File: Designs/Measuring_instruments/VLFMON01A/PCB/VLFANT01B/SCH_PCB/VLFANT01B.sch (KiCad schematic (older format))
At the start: 15 parts, among them J1 RJ45_RJHSE-5384, J2 RJ45_RJHSE-5384, J3 RJ45_RJHSE-5384, J7 SMA, J9 JUMP_3X2, M1 HOLE, M10 HOLE, M2 HOLE, M3 HOLE, M4 HOLE, M5 HOLE, M6 HOLE, M7 HOLE, M8 HOLE, M9 HOLE

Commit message: zmena
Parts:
- removed M10, M5, M6, M7, M8, M9: HOLE, Mlab_Mechanical:MountingHole_3mm, symbol HOLE
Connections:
- net OUT1: now also J3.4; no longer J3.1
- net OUT2: now also J3.5; no longer J3.2
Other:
- moved on the sheet: M1, M2, M3, M4

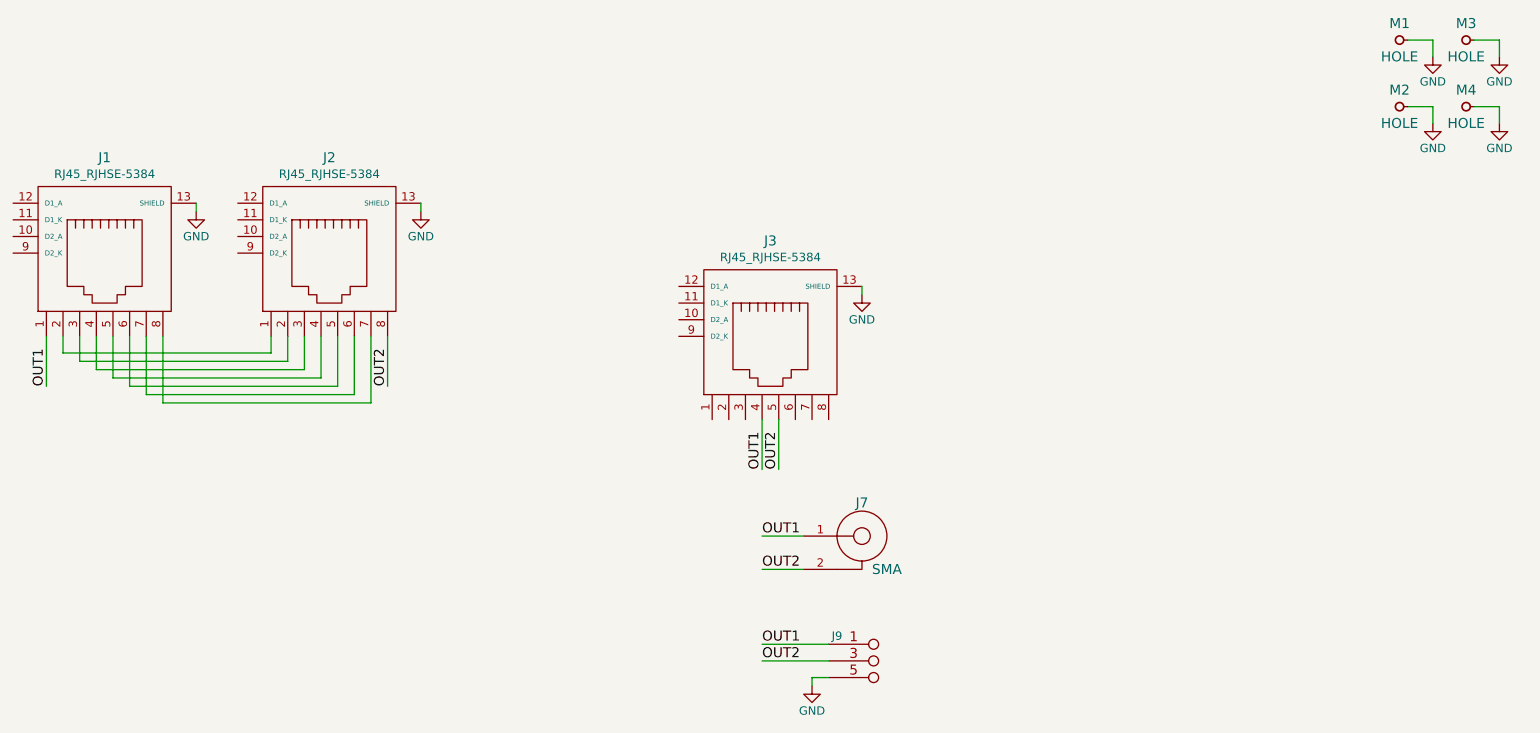
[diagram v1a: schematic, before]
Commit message: 
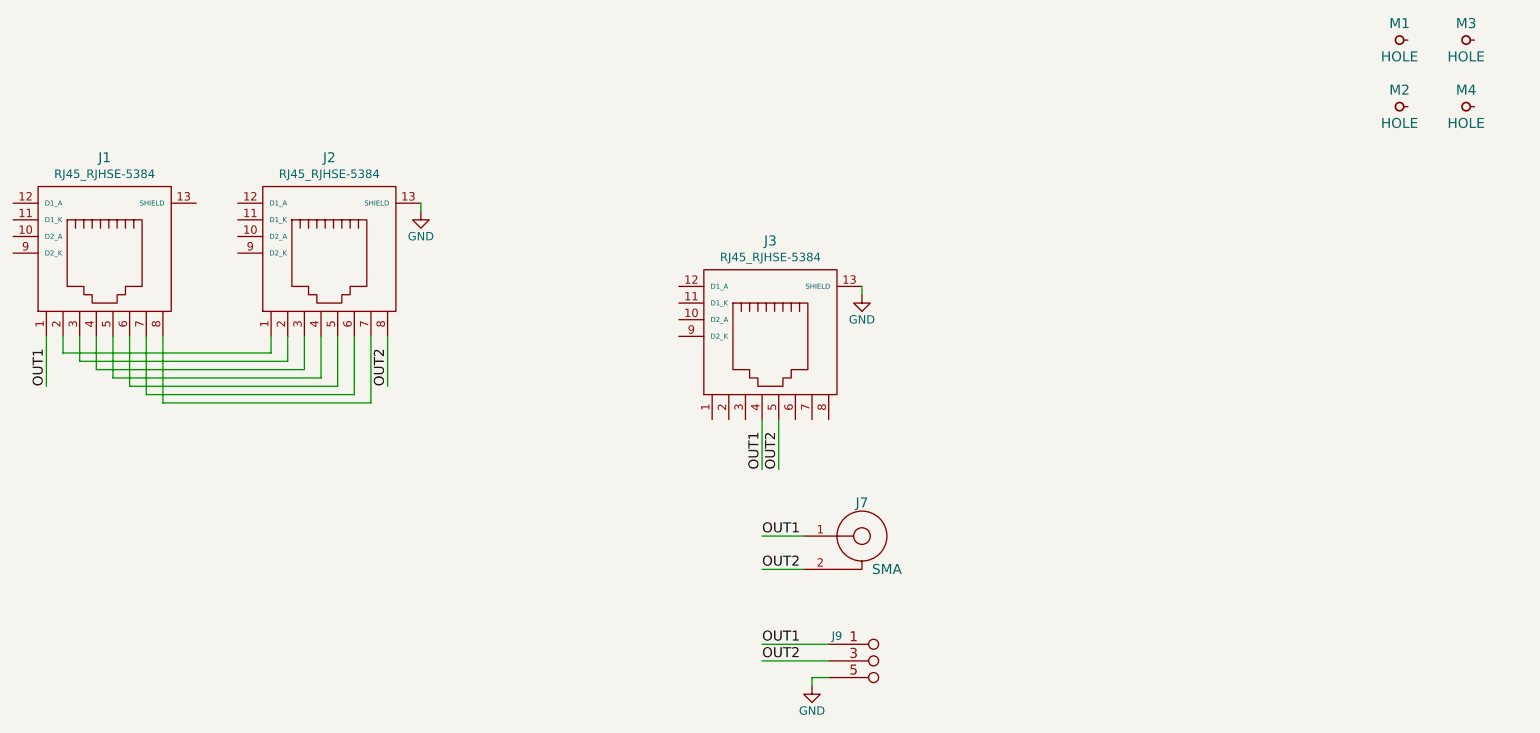
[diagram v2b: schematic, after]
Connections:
- net GND: no longer J1.13 (SHIELD), M1.1, M2.1, M3.1, M4.1
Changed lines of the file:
@@
 EESchema Schematic File Version 2
+LIBS:MLAB_BATERY
+LIBS:MLAB_CONNECTORS
+LIBS:MLAB_D
+LIBS:MLAB_DISPLAY
+LIBS:MLAB_IO
+LIBS:MLAB_Jumpers
+LIBS:MLAB_SW
+LIBS:MLAB_T
+LIBS:MLAB_U
 LIBS:74xgxx
 LIBS:74xx
-LIBS:ac-dc
 LIBS:actel
 LIBS:adc-dac
@@
 LIBS:brooktre
 LIBS:cmos4000
-LIBS:cmos_ieee
 LIBS:conn
 LIBS:contrib
@@
 LIBS:display
 LIBS:dsp
-LIBS:elec-unifil
 LIBS:ESD_Protection
 LIBS:ftdi
 LIBS:gennum
-LIBS:graphic
 LIBS:hc11
 LIBS:intel
@@
 LIBS:microchip_pic32mcu
 LIBS:microcontrollers
+LIBS:mlab_header
+LIBS:mlab_mechanical
 LIBS:motor_drivers
 LIBS:motorola
@@
 LIBS:transf
 LIBS:transistors
-LIBS:ttl_ieee
 LIBS:valves
 LIBS:video
 LIBS:Xicor
-LIBS:xilinx
 LIBS:Zilog
 LIBS:VLFANT01B-cache
@@
 $EndComp
 $Comp
-L GND #PWR01
-U 1 1 57D29BFA
-P 10480 820
-F 0 "#PWR01" H 10480 570 50  0001 C CNN
-F 1 "GND" H 10480 670 50  0000 C CNN
-F 2 "" H 10480 820 50  0000 C CNN
-F 3 "" H 10480 820 50  0000 C CNN
-	1    10480 820
-	1    0    0    -1
-$EndComp
-$Comp
 L HOLE M3
 U 1 1 57D2A075
@@
 $EndComp
 $Comp
-L GND #PWR02
-U 1 1 57D2A07B
-P 10880 820
-F 0 "#PWR02" H 10880 570 50  0001 C CNN
-F 1 "GND" H 10880 670 50  0000 C CNN
-F 2 "" H 10880 820 50  0000 C CNN
-F 3 "" H 10880 820 50  0000 C CNN
-	1    10880 820
-	1    0    0    -1
-$EndComp
-$Comp
 L HOLE M2
 U 1 1 57D2A387
@@
 $EndComp
 $Comp
-L GND #PWR03
-U 1 1 57D2A38D
-P 10480 1220
-F 0 "#PWR03" H 10480 970 50  0001 C CNN
-F 1 "GND" H 10480 1070 50  0000 C CNN
-F 2 "" H 10480 1220 50  0000 C CNN
-F 3 "" H 10480 1220 50  0000 C CNN
-	1    10480 1220
-	1    0    0    -1
-$EndComp
-$Comp
 L HOLE M4
 U 1 1 57D2A395
@@
 $EndComp
 $Comp
-L GND #PWR04
-U 1 1 57D2A39B
-P 10880 1220
-F 0 "#PWR04" H 10880 970 50  0001 C CNN
-F 1 "GND" H 10880 1070 50  0000 C CNN
-F 2 "" H 10880 1220 50  0000 C CNN
-F 3 "" H 10880 1220 50  0000 C CNN
-	1    10880 1220
-	1    0    0    -1
-$EndComp
-Wire Wire Line
-	10330 720  10480 720
-Wire Wire Line
-	10480 720  10480 820
-Wire Wire Line
-	10730 720  10880 720
-Wire Wire Line
-	10880 720  10880 820
-Wire Wire Line
-	10330 1120 10480 1120
-Wire Wire Line
-	10480 1120 10480 1220
-Wire Wire Line
-	10730 1120 10880 1120
-Wire Wire Line
-	10880 1120 10880 1220
-$Comp
 L SMA J7
 U 1 1 57D68C46
@@
 	6750 4550 6850 4550
 $Comp
+L RJ45_RJHSE-5384 J2
+U 1 1 58171334
+P 3850 2050
+F 0 "J2" H 3850 2674 60  0000 C CNN
+F 1 "RJ45_RJHSE-5384" H 3850 2575 51  0000 C CNN
+F 2 "Mlab_CON:RJHSE-5384(RJ45)" H 3850 2050 60  0001 C CNN
+F 3 "" H 3850 2050 60  0000 C CNN
+	1    3850 2050
+	1    0    0    -1
+$EndComp
+$Comp
+L RJ45_RJHSE-5384 J3
+U 1 1 58171450
+P 6500 2550
+F 0 "J3" H 6500 3174 60  0000 C CNN
+F 1 "RJ45_RJHSE-5384" H 6500 3075 51  0000 C CNN
+F 2 "Mlab_CON:RJHSE-5384(RJ45)" H 6500 2550 60  0001 C CNN
+F 3 "" H 6500 2550 60  0000 C CNN
+	1    6500 2550
+	1    0    0    -1
+$EndComp
+Text Label 2150 2800 1    60   ~ 0
+OUT1
+Wire Wire Line
+	2150 2500 2150 2800
+Wire Wire Line
+	3500 2500 3500 2600
+Wire Wire Line
+	3500 2600 2250 2600
+Wire Wire Line
+	2250 2600 2250 2500
+Wire Wire Line
+	3600 2500 3600 2650
+Wire Wire Line
+	3600 2650 2350 2650
+Wire Wire Line
+	2350 2650 2350 2500
+Wire Wire Line
+	3700 2500 3700 2700
+Wire Wire Line
+	3700 2700 2450 2700
+Wire Wire Line
+	2450 2700 2450 2500
+Wire Wire Line
+	3800 2500 3800 2750
+Wire Wire Line
+	3800 2750 2550 2750
+Wire Wire Line
+	2550 2750 2550 2500
+Wire Wire Line
+	3900 2500 3900 2800
+Wire Wire Line
+	3900 2800 2650 2800
+Wire Wire Line
+	2650 2800 2650 2500
+Wire Wire Line
+	4000 2500 4000 2850
+Wire Wire Line
+	4000 2850 2750 2850
+Wire Wire Line
+	2750 2850 2750 2500
+Wire Wire Line
+	4100 2500 4100 2900
+Wire Wire Line
+	4100 2900 2850 2900
+Wire Wire Line
+	2850 2900 2850 2500
+Text Label 4200 2800 1    60   ~ 0
+OUT2
+Wire Wire Line
+	4200 2500 4200 2800
+$Comp
+L GND #PWR013
+U 1 1 581734D2
+P 4400 1750
+F 0 "#PWR013" H 4400 1500 50  0001 C CNN
+F 1 "GND" H 4400 1600 50  0000 C CNN
+F 2 "" H 4400 1750 50  0000 C CNN
+F 3 "" H 4400 1750 50  0000 C CNN
+	1    4400 1750
+	1    0    0    -1
+$EndComp
+Wire Wire Line
+	4400 1750 4400 1700
+Text Label 6450 3300 1    60   ~ 0
+OUT1
+Text Label 6550 3300 1    60   ~ 0
+OUT2
+Wire Wire Line
+	6450 3300 6450 3000
+Wire Wire Line
+	6550 3300 6550 3000
+$Comp
+L GND #PWR014
+U 1 1 581755DF
+P 7050 2250
+F 0 "#PWR014" H 7050 2000 50  0001 C CNN
+F 1 "GND" H 7050 2100 50  0000 C CNN
+F 2 "" H 7050 2250 50  0000 C CNN
+F 3 "" H 7050 2250 50  0000 C CNN
+	1    7050 2250
+	1    0    0    -1
+$EndComp
+Wire Wire Line
+	7050 2250 7050 2200
+$Comp
 L RJ45_RJHSE-5384 J1
 U 1 1 58170EC6
@@
 	1    0    0    -1
 $EndComp
-$Comp
-L RJ45_RJHSE-5384 J2
-U 1 1 58171334
-P 3850 2050
-F 0 "J2" H 3850 2674 60  0000 C CNN
-F 1 "RJ45_RJHSE-5384" H 3850 2575 51  0000 C CNN
-F 2 "Mlab_CON:RJHSE-5384(RJ45)" H 3850 2050 60  0001 C CNN
-F 3 "" H 3850 2050 60  0000 C CNN
-	1    3850 2050
-	1    0    0    -1
-$EndComp
-$Comp
-L RJ45_RJHSE-5384 J3
-U 1 1 58171450
-P 6500 2550
-F 0 "J3" H 6500 3174 60  0000 C CNN
-F 1 "RJ45_RJHSE-5384" H 6500 3075 51  0000 C CNN
-F 2 "Mlab_CON:RJHSE-5384(RJ45)" H 6500 2550 60  0001 C CNN
-F 3 "" H 6500 2550 60  0000 C CNN
-	1    6500 2550
-	1    0    0    -1
-$EndComp
-Text Label 2150 2800 1    60   ~ 0
-OUT1
-Wire Wire Line
-	2150 2500 2150 2800
-Wire Wire Line
-	3500 2500 3500 2600
-Wire Wire Line
-	3500 2600 2250 2600
-Wire Wire Line
-	2250 2600 2250 2500
-Wire Wire Line
-	3600 2500 3600 2650
-Wire Wire Line
-	3600 2650 2350 2650
-Wire Wire Line
-	2350 2650 2350 2500
-Wire Wire Line
-	3700 2500 3700 2700
-Wire Wire Line
-	3700 2700 2450 2700
-Wire Wire Line
-	2450 2700 2450 2500
-Wire Wire Line
-	3800 2500 3800 2750
-Wire Wire Line
-	3800 2750 2550 2750
-Wire Wire Line
-	2550 2750 2550 2500
-Wire Wire Line
-	3900 2500 3900 2800
-Wire Wire Line
-	3900 2800 2650 2800
-Wire Wire Line
-	2650 2800 2650 2500
-Wire Wire Line
-	4000 2500 4000 2850
-Wire Wire Line
-	4000 2850 2750 2850
-Wire Wire Line
-	2750 2850 2750 2500
-Wire Wire Line
-	4100 2500 4100 2900
-Wire Wire Line
-	4100 2900 2850 2900
-Wire Wire Line
-	2850 2900 2850 2500
-Text Label 4200 2800 1    60   ~ 0
-OUT2
-Wire Wire Line
-	4200 2500 4200 2800
-$Comp
-L GND #PWR012
-U 1 1 58173397
-P 3050 1750
-F 0 "#PWR012" H 3050 1500 50  0001 C CNN
-F 1 "GND" H 3050 1600 50  0000 C CNN
-F 2 "" H 3050 1750 50  0000 C CNN
-F 3 "" H 3050 1750 50  0000 C CNN
-	1    3050 1750
-	1    0    0    -1
-$EndComp
-$Comp
-L GND #PWR013
-U 1 1 581734D2
-P 4400 1750
-F 0 "#PWR013" H 4400 1500 50  0001 C CNN
-F 1 "GND" H 4400 1600 50  0000 C CNN
-F 2 "" H 4400 1750 50  0000 C CNN
-F 3 "" H 4400 1750 50  0000 C CNN
-	1    4400 1750
-	1    0    0    -1
-$EndComp
-Wire Wire Line
-	4400 1750 4400 1700
-Wire Wire Line
-	3050 1750 3050 1700
-Text Label 6450 3300 1    60   ~ 0
-OUT1
-Text Label 6550 3300 1    60   ~ 0
-OUT2
-Wire Wire Line
-	6450 3300 6450 3000
-Wire Wire Line
-	6550 3300 6550 3000
-$Comp
-L GND #PWR014
-U 1 1 581755DF
-P 7050 2250
-F 0 "#PWR014" H 7050 2000 50  0001 C CNN
-F 1 "GND" H 7050 2100 50  0000 C CNN
-F 2 "" H 7050 2250 50  0000 C CNN
-F 3 "" H 7050 2250 50  0000 C CNN
-	1    7050 2250
-	1    0    0    -1
-$EndComp
-Wire Wire Line
-	7050 2250 7050 2200
 $EndSCHEMATC
